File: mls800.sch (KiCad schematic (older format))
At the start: 48 parts, among them CON1 BARREL_JACK, IC1 6N137, J1 USB, P1 CONN_02X03, P2 DIN_5, P3 DIN_5, SW1 SW_TACT_LED, SW10 SW_TACT_LED, SW11 SW_TACT_LED, U1 LM340MP-5.0/NOPB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

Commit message: MLS800
* routing : core pcb & components
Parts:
- removed R5, R8: 1k, Resistors_SMD:R_0805_HandSoldering, symbol R
- removed R7: 10K, Resistors_SMD:R_0805_HandSoldering, symbol R
- removed SW10, SW11: SW_TACT_LED, Custom-device:MEC-5G, symbol SW_TACT_LED
- added P4: CONN_02X03, Pin_Headers:Pin_Header_Straight_2x03, symbol CONN_02X03
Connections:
- net labels added: EDIT_LED
- wire segments 106 -> 114

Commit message: MLS800
* schematic : changed all 1n4148 to bournes references
 * changed footprints to match bournes ones
 * re routed all the loops part of the pcb
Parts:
- D1, D5: value 1N4148 -> CD1206-S01575; footprint Imported:SOD-123 -> SMD_Packages:SMD-1206_Pol
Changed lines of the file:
@@
 P 1700 1250
 F 0 "D1" H 1700 1350 40  0000 C CNN
-F 1 "1N4148" H 1700 1150 40  0000 C CNN
-F 2 "Imported:SOD-123" H 1700 1250 60  0001 C CNN
+F 1 "CD1206-S01575" H 1700 1150 40  0000 C CNN
+F 2 "SMD_Packages:SMD-1206_Pol" H 1700 1250 60  0001 C CNN
 F 3 "~" H 1700 1250 60  0000 C CNN
 	1    1700 1250
@@
 P 9350 2050
 F 0 "D5" H 9350 2150 40  0000 C CNN
-F 1 "1N4148" H 9350 1950 40  0000 C CNN
-F 2 "Imported:SOD-123" H 9350 2050 60  0001 C CNN
+F 1 "CD1206-S01575" H 9350 1950 40  0000 C CNN
+F 2 "SMD_Packages:SMD-1206_Pol" H 9350 2050 60  0001 C CNN
 F 3 "~" H 9350 2050 60  0000 C CNN
 	1    9350 2050

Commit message: MLS800
* unsplit AGND and DGND
* retouted relays
* relayout of gnd zone
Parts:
- removed R2, R3: 0, Resistors_SMD:R_0805_HandSoldering, symbol R
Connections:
- net labels removed: AGND, DGND
- wire segments 114 -> 111

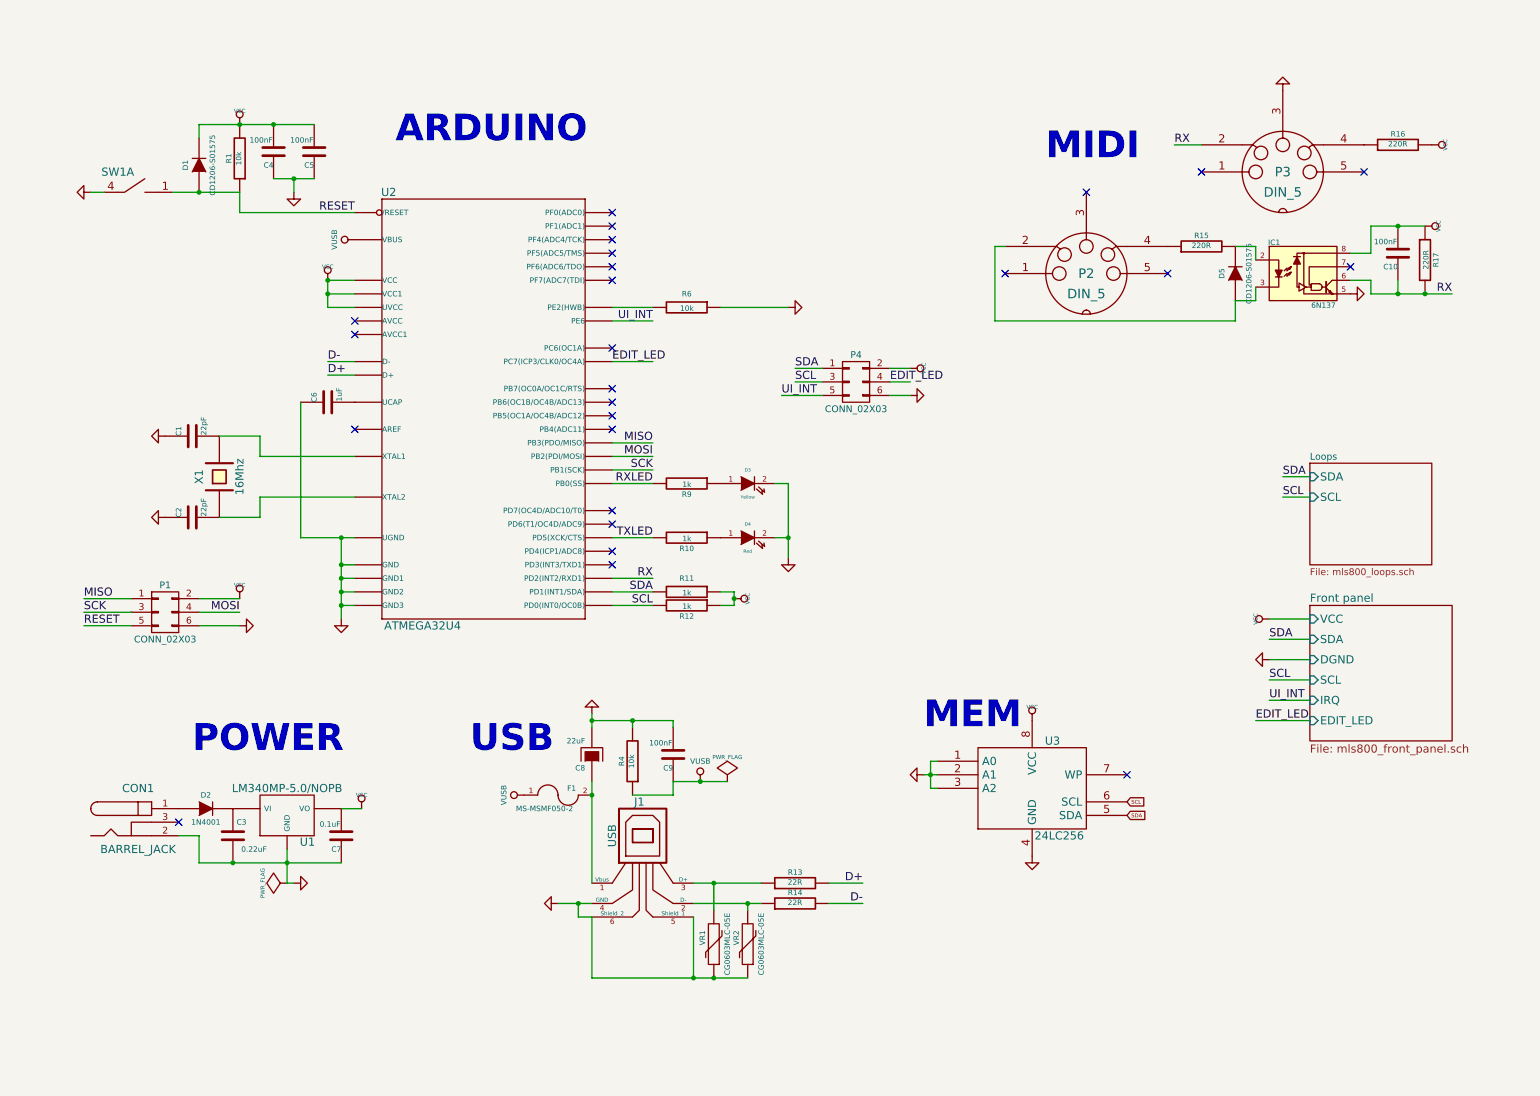
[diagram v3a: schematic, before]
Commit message: MLS800
* rerouting
* copper zones
* layout optimization
* pcb size reduction
* change u2 to internal kicad library (may induce error in layout, this commit comes just before applying netlist)
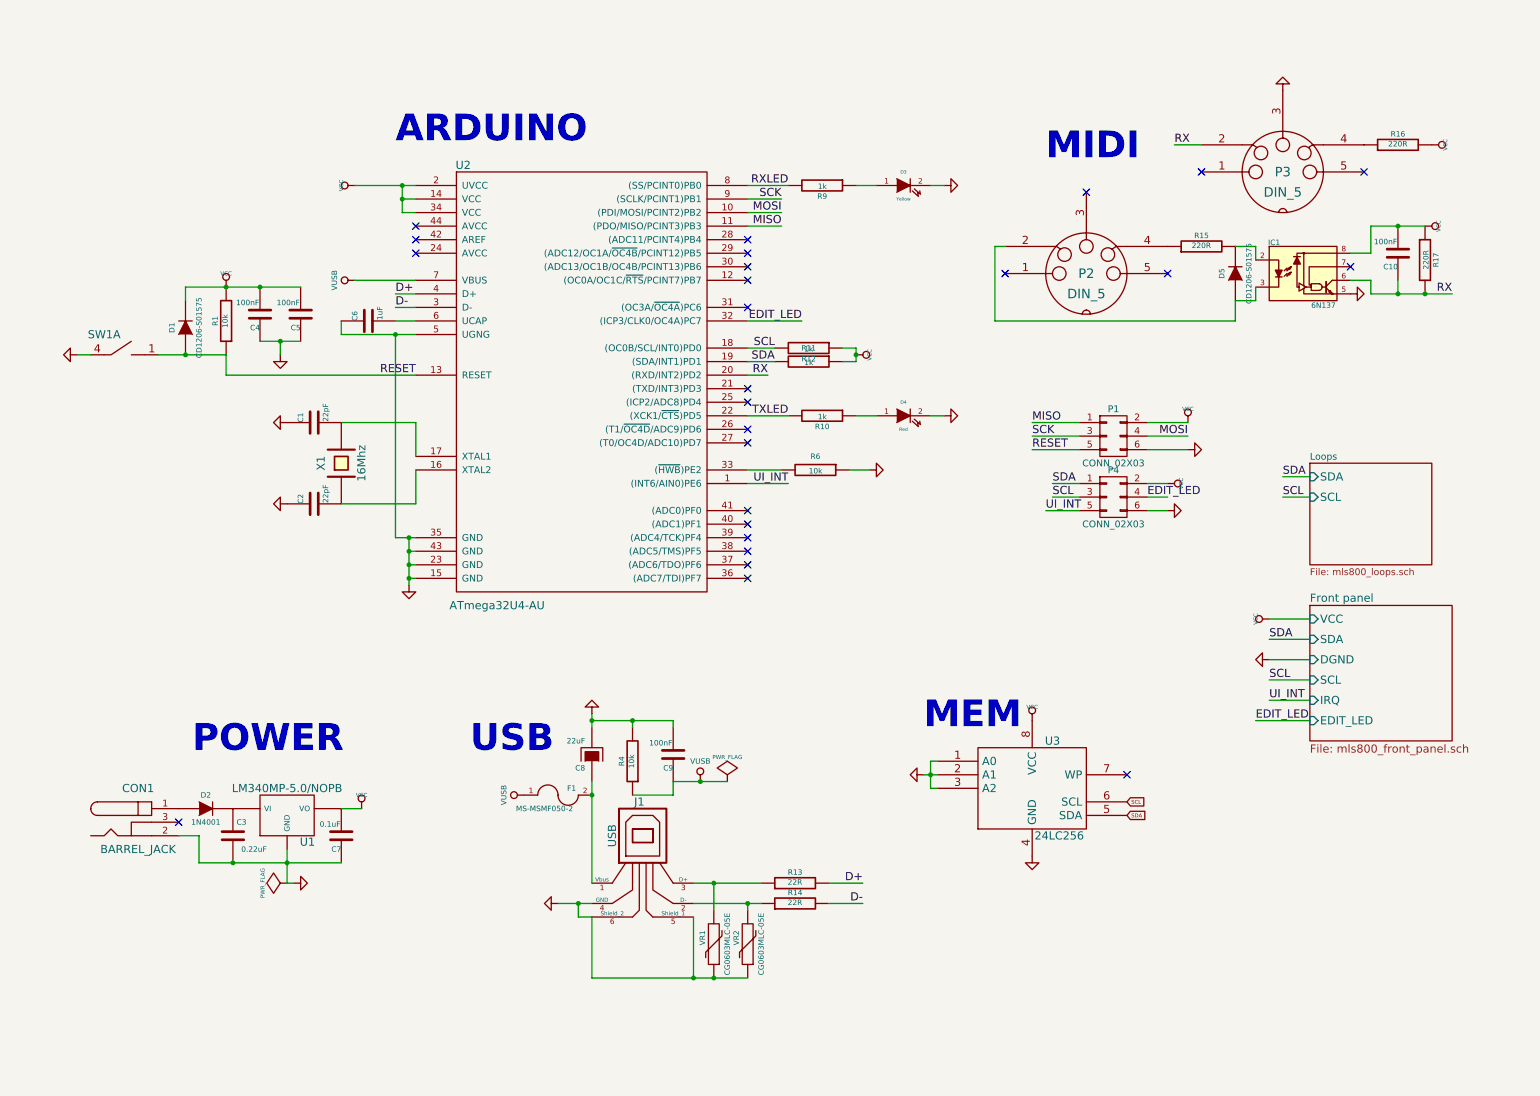
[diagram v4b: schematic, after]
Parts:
- removed U2: ATMEGA32U4, Housings_QFP:TQFP-44_10x10mm_Pitch0.8mm, symbol ATMEGA32U4
- added U2: ATmega32U4-AU, Housings_QFP:TQFP-44_10x10mm_Pitch0.8mm, symbol ATmega32U4-AU
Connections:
- net D+: now also U2.4 (D+)
- net D-: now also U2.3 (D-)
- net EDIT_LED: now also U2.32 ((ICP3/CLK0/OC4A)PC7)
- net GND: now also U2.15 (GND), U2.23 (GND), U2.35 (GND), U2.43 (GND), U2.5 (UGNG)
- net MISO: now also U2.11 ((PDO/MISO/PCINT3)PB3)
- net MOSI: now also U2.10 ((PDI/MOSI/PCINT2)PB2)
- net RESET: now also U2.13 (RESET)
- net RX: now also U2.20 ((RXD/INT2)PD2)
- net RXLED: now also U2.8 ((SS/PCINT0)PB0)
- net SCK: now also U2.9 ((SCLK/PCINT1)PB1)
- net SCL: now also U2.18 ((OC0B/SCL/INT0)PD0)
- net SDA: now also U2.19 ((SDA/INT1)PD1)
- net TXLED: now also U2.22 ((XCK1/~CTS~)PD5)
- net UI_INT: now also U2.1 ((INT6/AIN0)PE6)
- net VCC: now also U2.14 (VCC), U2.2 (UVCC), U2.34 (VCC)
- net VCOM: now also U2.7 (VBUS)
- net at C2.2, X1.1: now also U2.16 (XTAL2)
- net at C1.2, X1.2: now also U2.17 (XTAL1)
- net at C6.2: now also U2.6 (UCAP)
- net at R6.2: now also U2.33 ((~HWB~)PE2)
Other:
- moved on the sheet: C1, C2, C4, C5, C6, D1, D3, D4, P1, P4, R1, R10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

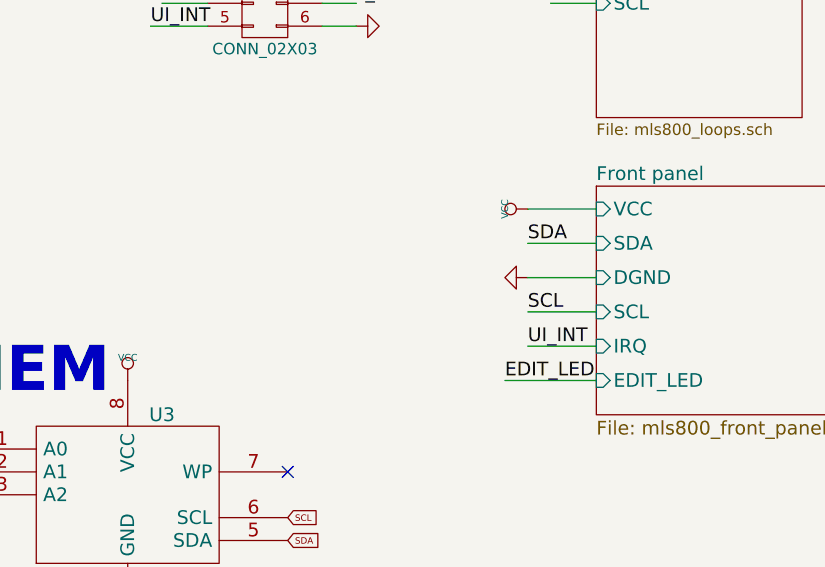
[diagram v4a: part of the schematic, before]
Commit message: MLS800
* splitted schematics for DRC tests
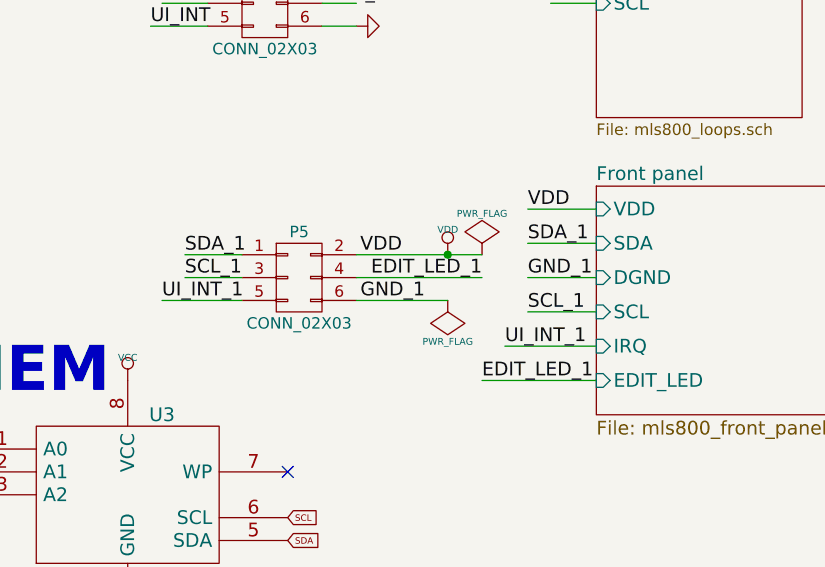
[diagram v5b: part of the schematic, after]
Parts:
- added P5: CONN_02X03, Pin_Headers:Pin_Header_Straight_2x03, symbol CONN_02X03
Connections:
- new net EDIT_LED_1: P5.4 (P4)
- new net GND_1: P5.6 (P6)
- new net SCL_1: P5.3 (P3)
- new net SDA_1: P5.1 (P1)
- new net UI_INT_1: P5.5 (P5)
- new net VDD: P5.2 (P2)
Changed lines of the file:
@@
 F3 "SCL" I L 9900 5050 60
 F4 "IRQ" I L 9900 5200 60
-F5 "VCC" I L 9900 4600 60
+F5 "VDD" I L 9900 4600 60
 F6 "DGND" I L 9900 4900 60
 F7 "EDIT_LED" I L 9900 5350 60
 $EndSheet
+Text Label 9600 4750 0    60   ~ 0
+SDA_1
+Text Label 9600 5050 0    60   ~ 0
+SCL_1
+Text Label 9500 5200 0    60   ~ 0
+UI_INT_1
+Text Label 9400 5350 0    60   ~ 0
+EDIT_LED_1
 $Comp
 L VCC #PWR011
-U 1 1 549792C2
-P 9600 4600
-F 0 "#PWR011" H 9600 4700 30  0001 C CNN
-F 1 "VCC" H 9600 4700 30  0000 C CNN
-F 2 "" H 9600 4600 60  0000 C CNN
-F 3 "" H 9600 4600 60  0000 C CNN
-	1    9600 4600
-	0    -1   -1   0
-$EndComp
-Text Label 9600 4750 0    60   ~ 0
-SDA
-Text Label 9600 5050 0    60   ~ 0
-SCL
-Text Label 9600 5200 0    60   ~ 0
-UI_INT
-Text Label 9500 5350 0    60   ~ 0
-EDIT_LED
-$Comp
-L VCC #PWR012
 U 1 1 5497A226
 P 8850 3600
-F 0 "#PWR012" H 8850 3700 30  0001 C CNN
+F 0 "#PWR011" H 8850 3700 30  0001 C CNN
 F 1 "VCC" H 8850 3700 30  0000 C CNN
 F 2 "" H 8850 3600 60  0000 C CNN
@@
 SCL
 $Comp
-L GND #PWR013
-U 1 1 54B71FFA
-P 9600 4900
-F 0 "#PWR013" H 9600 4900 30  0001 C CNN
-F 1 "GND" H 9600 4830 30  0001 C CNN
-F 2 "" H 9600 4900 60  0000 C CNN
-F 3 "" H 9600 4900 60  0000 C CNN
-	1    9600 4900
-	0    1    1    0
-$EndComp
-$Comp
-L GND #PWR014
+L GND #PWR012
 U 1 1 54B72617
 P 9700 700
-F 0 "#PWR014" H 9700 700 30  0001 C CNN
+F 0 "#PWR012" H 9700 700 30  0001 C CNN
 F 1 "GND" H 9700 630 30  0001 C CNN
 F 2 "" H 9700 700 60  0000 C CNN
@@
 $EndComp
 $Comp
-L GND #PWR015
+L GND #PWR013
 U 1 1 54B732E3
 P 9000 3350
-F 0 "#PWR015" H 9000 3350 30  0001 C CNN
+F 0 "#PWR013" H 9000 3350 30  0001 C CNN
 F 1 "GND" H 9000 3280 30  0001 C CNN
 F 2 "" H 9000 3350 60  0000 C CNN
@@
 $EndComp
 $Comp
-L GND #PWR016
+L GND #PWR014
 U 1 1 54B73920
 P 4600 5300
-F 0 "#PWR016" H 4600 5300 30  0001 C CNN
+F 0 "#PWR014" H 4600 5300 30  0001 C CNN
 F 1 "GND" H 4600 5230 30  0001 C CNN
 F 2 "" H 4600 5300 60  0000 C CNN
@@
 $EndComp
 $Comp
-L GND #PWR017
+L GND #PWR015
 U 1 1 54B73B37
 P 4350 6700
-F 0 "#PWR017" H 4350 6700 30  0001 C CNN
+F 0 "#PWR015" H 4350 6700 30  0001 C CNN
 F 1 "GND" H 4350 6630 30  0001 C CNN
 F 2 "" H 4350 6700 60  0000 C CNN
@@
 $EndComp
 $Comp
-L GND #PWR018
+L GND #PWR016
 U 1 1 54B743C1
 P 800 2650
-F 0 "#PWR018" H 800 2650 30  0001 C CNN
+F 0 "#PWR016" H 800 2650 30  0001 C CNN
 F 1 "GND" H 800 2580 30  0001 C CNN
 F 2 "" H 800 2650 60  0000 C CNN
@@
 $EndComp
 $Comp
-L GND #PWR019
+L GND #PWR017
 U 1 1 54B74982
 P 2300 2650
-F 0 "#PWR019" H 2300 2650 30  0001 C CNN
+F 0 "#PWR017" H 2300 2650 30  0001 C CNN
 F 1 "GND" H 2300 2580 30  0001 C CNN
 F 2 "" H 2300 2650 60  0000 C CNN
@@
 $EndComp
 $Comp
-L GND #PWR020
+L GND #PWR018
 U 1 1 54B75B76
 P 8850 3800
-F 0 "#PWR020" H 8850 3800 30  0001 C CNN
+F 0 "#PWR018" H 8850 3800 30  0001 C CNN
 F 1 "GND" H 8850 3730 30  0001 C CNN
 F 2 "" H 8850 3800 60  0000 C CNN
@@
 $EndComp
 $Comp
-L GND #PWR021
+L GND #PWR019
 U 1 1 54B7635C
 P 10200 2200
-F 0 "#PWR021" H 10200 2200 30  0001 C CNN
+F 0 "#PWR019" H 10200 2200 30  0001 C CNN
 F 1 "GND" H 10200 2130 30  0001 C CNN
 F 2 "" H 10200 2200 60  0000 C CNN
@@
 $EndComp
 $Comp
-L GND #PWR022
+L GND #PWR020
 U 1 1 54B6F74A
 P 7850 6350
-F 0 "#PWR022" H 7850 6350 30  0001 C CNN
+F 0 "#PWR020" H 7850 6350 30  0001 C CNN
 F 1 "GND" H 7850 6280 30  0001 C CNN
 F 2 "" H 7850 6350 60  0000 C CNN
@@
 $EndComp
 $Comp
-L GND #PWR023
+L GND #PWR021
 U 1 1 54B6F786
 P 7050 5750
-F 0 "#PWR023" H 7050 5750 30  0001 C CNN
+F 0 "#PWR021" H 7050 5750 30  0001 C CNN
 F 1 "GND" H 7050 5680 30  0001 C CNN
 F 2 "" H 7050 5750 60  0000 C CNN
@@
 $EndComp
 $Comp
-L GND #PWR024
+L GND #PWR022
 U 1 1 54B6FB8E
 P 2350 3750
-F 0 "#PWR024" H 2350 3750 30  0001 C CNN
+F 0 "#PWR022" H 2350 3750 30  0001 C CNN
 F 1 "GND" H 2350 3680 30  0001 C CNN
 F 2 "" H 2350 3750 60  0000 C CNN
@@
 $EndComp
 $Comp
-L GND #PWR025
+L GND #PWR023
 U 1 1 54B6FBCA
 P 2350 3150
-F 0 "#PWR025" H 2350 3150 30  0001 C CNN
+F 0 "#PWR023" H 2350 3150 30  0001 C CNN
 F 1 "GND" H 2350 3080 30  0001 C CNN
 F 2 "" H 2350 3150 60  0000 C CNN
@@
 $EndComp
 $Comp
-L GND #PWR026
+L GND #PWR024
 U 1 1 54BC85DD
 P 3250 4350
-F 0 "#PWR026" H 3250 4350 30  0001 C CNN
+F 0 "#PWR024" H 3250 4350 30  0001 C CNN
 F 1 "GND" H 3250 4280 30  0001 C CNN
 F 2 "" H 3250 4350 60  0000 C CNN
@@
 NoConn ~ 3300 1700
 $Comp
-L VCC #PWR027
+L VCC #PWR025
 U 1 1 54BCB5AE
 P 2850 1400
-F 0 "#PWR027" H 2850 1500 30  0001 C CNN
+F 0 "#PWR025" H 2850 1500 30  0001 C CNN
 F 1 "VCC" H 2850 1500 30  0000 C CNN
 F 2 "" H 2850 1400 60  0000 C CNN
@@
 $EndComp
 $Comp
-L GND #PWR028
+L GND #PWR026
 U 1 1 54BCE6C7
 P 6650 3500
-F 0 "#PWR028" H 6650 3500 30  0001 C CNN
+F 0 "#PWR026" H 6650 3500 30  0001 C CNN
 F 1 "GND" H 6650 3430 30  0001 C CNN
 F 2 "" H 6650 3500 60  0000 C CNN
@@
 RXLED
 $Comp
-L GND #PWR029
+L GND #PWR027
 U 1 1 54BD0A4D
 P 7200 3100
-F 0 "#PWR029" H 7200 3100 30  0001 C CNN
+F 0 "#PWR027" H 7200 3100 30  0001 C CNN
 F 1 "GND" H 7200 3030 30  0001 C CNN
 F 2 "" H 7200 3100 60  0000 C CNN
@@
 $EndComp
 $Comp
-L GND #PWR030
+L GND #PWR028
 U 1 1 54BD0A83
 P 7200 1400
-F 0 "#PWR030" H 7200 1400 30  0001 C CNN
+F 0 "#PWR028" H 7200 1400 30  0001 C CNN
 F 1 "GND" H 7200 1330 30  0001 C CNN
 F 2 "" H 7200 1400 60  0000 C CNN
@@
 	9900 4900 9600 4900
 Wire Wire Line
-	9900 5200 9600 5200
-Wire Wire Line
-	9900 5350 9500 5350
+	9500 5200 9900 5200
+Wire Wire Line
+	9400 5350 9900 5350
 Wire Wire Line
 	8700 3600 8850 3600
@@
 Text Label 7950 3800 0    60   ~ 0
 UI_INT
+$Comp
+L CONN_02X03 P5
+U 1 1 54BF26D9
+P 8600 4900
+F 0 "P5" H 8600 5100 50  0000 C CNN
+F 1 "CONN_02X03" H 8600 4700 50  0000 C CNN
+F 2 "Pin_Headers:Pin_Header_Straight_2x03" H 8600 3700 60  0001 C CNN
+F 3 "" H 8600 3700 60  0000 C CNN
+	1    8600 4900
+	1    0    0    -1
+$EndComp
+Text Label 8100 4800 0    60   ~ 0
+SDA_1
+Text Label 8100 4900 0    60   ~ 0
+SCL_1
+Text Label 8000 5000 0    60   ~ 0
+UI_INT_1
+Text Label 9400 4900 2    60   ~ 0
+EDIT_LED_1
+Wire Wire Line
+	8850 4900 9400 4900
+Wire Wire Line
+	8350 4900 8100 4900
+Wire Wire Line
+	8100 4800 8350 4800
+Wire Wire Line
+	8000 5000 8350 5000
+Wire Wire Line
+	8850 4800 9400 4800
+Wire Wire Line
+	8850 5000 9250 5000
+Text Label 9050 4800 2    60   ~ 0
+VDD
+Text Label 9150 5000 2    60   ~ 0
+GND_1
+Text Label 9600 4600 0    60   ~ 0
+VDD
+Text Label 9600 4900 0    60   ~ 0
+GND_1
+$Comp
+L PWR_FLAG #FLG029
+U 1 1 54BF6034
+P 9250 5000
+F 0 "#FLG029" H 9250 5095 30  0001 C CNN
+F 1 "PWR_FLAG" H 9250 5180 30  0000 C CNN
+F 2 "" H 9250 5000 60  0000 C CNN
+F 3 "" H 9250 5000 60  0000 C CNN
+	1    9250 5000
+	-1   0    0    1
+$EndComp
+$Comp
+L PWR_FLAG #FLG030
+U 1 1 54BF79C1
+P 9400 4800
+F 0 "#FLG030" H 9400 4895 30  0001 C CNN
+F 1 "PWR_FLAG" H 9400 4980 30  0000 C CNN
+F 2 "" H 9400 4800 60  0000 C CNN
+F 3 "" H 9400 4800 60  0000 C CNN
+	1    9400 4800
+	1    0    0    -1
+$EndComp
+$Comp
+L VDD #PWR031
+U 1 1 54BF7A12
+P 9250 4800
+F 0 "#PWR031" H 9250 4900 30  0001 C CNN
+F 1 "VDD" H 9250 4910 30  0000 C CNN
+F 2 "" H 9250 4800 60  0000 C CNN
+F 3 "" H 9250 4800 60  0000 C CNN
+	1    9250 4800
+	1    0    0    -1
+$EndComp
+Connection ~ 9250 4800
 $EndSCHEMATC

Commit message: MLS800
* changed D2 footprint according to availability
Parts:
- D2: footprint Diodes_SMD:Diode-SMB_Handsoldering -> Diodes_SMD:Diode-SMA_Handsoldering
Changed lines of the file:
@@
 F 0 "D2" H 1750 6100 40  0000 C CNN
 F 1 "1N4001" H 1750 5900 40  0000 C CNN
-F 2 "Diodes_SMD:Diode-SMB_Handsoldering" H 1750 6000 60  0001 C CNN
+F 2 "Diodes_SMD:Diode-SMA_Handsoldering" H 1750 6000 60  0001 C CNN
 F 3 "~" H 1750 6000 60  0000 C CNN
 	1    1750 6000
